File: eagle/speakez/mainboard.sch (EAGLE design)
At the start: 41 parts, among them U1 +12v

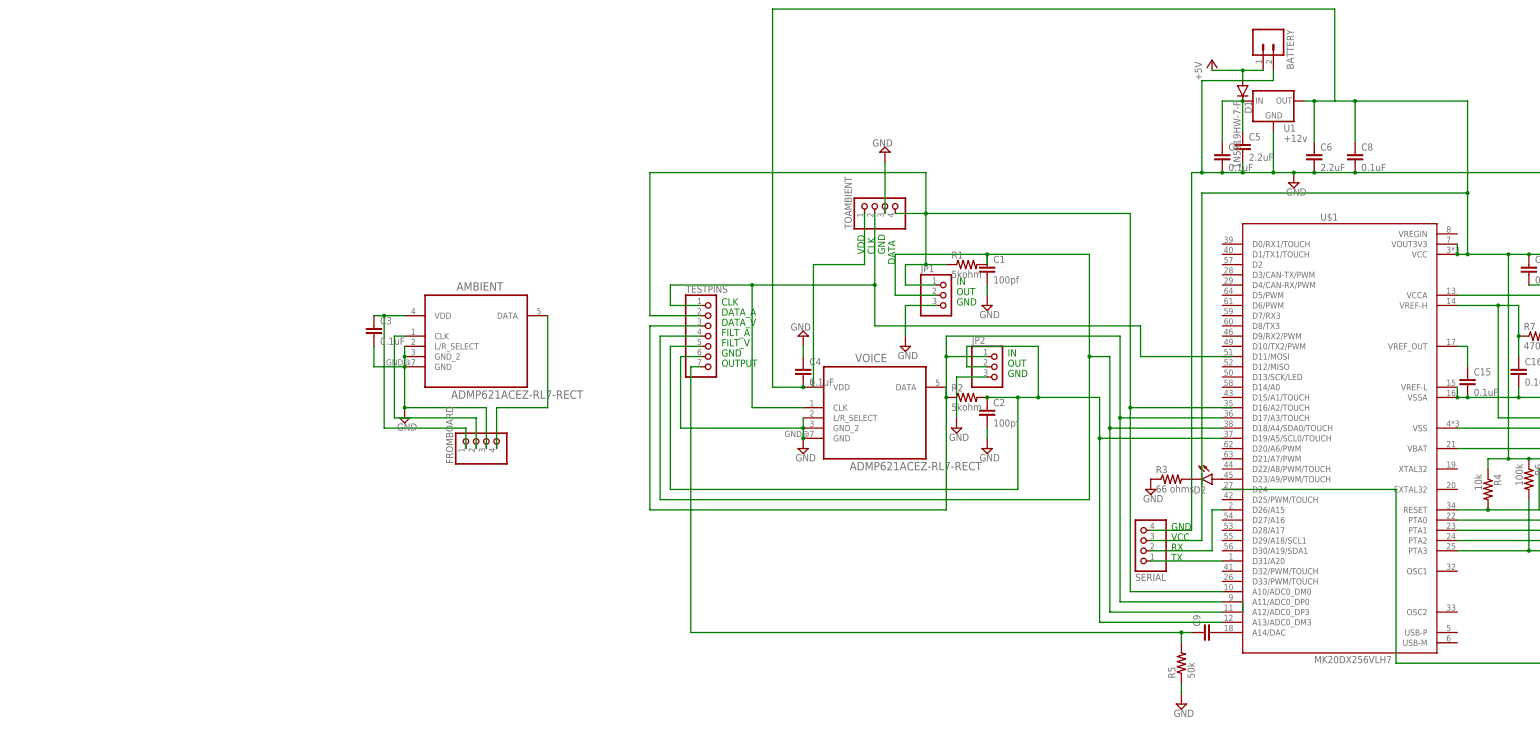
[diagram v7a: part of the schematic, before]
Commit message: corrected battery and voltage regulator
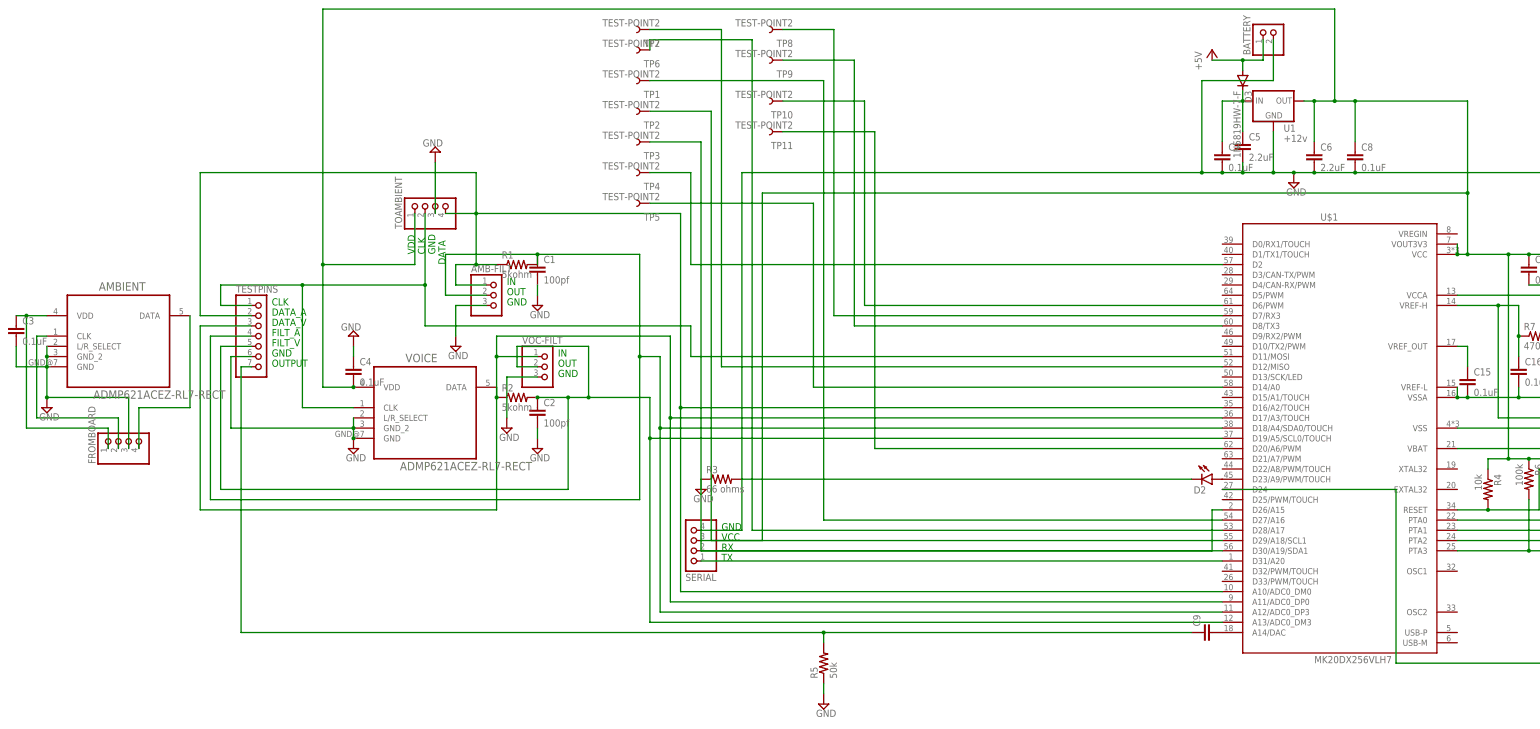
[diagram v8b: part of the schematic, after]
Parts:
- removed D1: 1N5819HW-7-F, SparkFun-DiscreteSemi:DIODESOD123
- removed JP1, JP2: (no value), pinhead:PINHD-1X3
- added AMB-FILT, VOC-FILT: (no value), pinhead:PINHD-1X3
- added D3: 1N5819HW-7-F, SparkFun-DiscreteSemi:DIODESOD123
- added TP1, TP10, TP11, TP2, TP3, TP4, TP5, TP6, TP7, TP8, TP9: TEST-POINT2, SparkFun-Passives:TEST-POINT2
- BATTERY: device SparkFun-Connectors:M02-JST-2-PTH-NO_SILK -> pinhead:PINHD-1X2
- U1: device SparkFun-PowerIC:V_REG_78XX7812 -> LP38691:V_REG_78XX7812
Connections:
- net N$6 renamed CLK2-A
- net N$7 renamed VDD-DECOUP-A
- net N$8 renamed DATA2-A
- removed net DECOUPLED: BK2125HM601-T.1, C10.1, C11.1, C12.1, C13.1, C14.1, C4.2, C6.1, C8.1, JLINK.1, R4.1, R6.1, SERIAL.3, TEST2.1, TEST2.6, TEST2.7, U$1.VBAT, U$1.VCC, U$1.VOUT3V3, U1.OUT, VOICE.VDD
- removed net TEST-PINS: TESTPINS.1, TOAMBIENT.2, VOICE.CLK
- new net CLK: TESTPINS.1, TOAMBIENT.2, U$1.D11/MOSI, VOICE.CLK
- new net DATA2: AMB-FILT.1, R1.1, TESTPINS.2, TOAMBIENT.4, U$1.A10/ADC0_DM0, U$1.D16/A2/TOUCH
- new net N$12: TP9.1, U$1.D8/TX3
- new net N$18: TP10.1, U$1.D6/PWM
- new net N$21: TP11.1, U$1.D20/A6/PWM
- new net N$3: TP7.1, U$1.D12/MISO
- new net N$4: TP6.1, U$1.D28/A17
- new net N$5: TP1.1, U$1.D27/A16
- new net N$6: TP2.1, U$1.D29/A18/SCL1
- new net N$7: TP3.1, U$1.D30/A19/SDA1
- new net N$8: TP4.1, U$1.D2
- new net VDD-DECOUP: BK2125HM601-T.1, C10.1, C11.1, C12.1, C13.1, C14.1, C4.2, C6.1, C8.1, JLINK.1, R4.1, R6.1, SERIAL.3, TEST2.1, TEST2.6, TEST2.7, TOAMBIENT.1, U$1.VBAT, U$1.VCC, U$1.VOUT3V3, U1.OUT, VOICE.VDD
- net +5V: now also D3.A; no longer D1.A
- net DATA: now also VOC-FILT.1; no longer JP2.1
- net GND: now also AMB-FILT.3, VOC-FILT.3; no longer JP1.3, JP2.3
- net N$1: now also AMB-FILT.2; no longer JP1.2
- net N$10: now also TP8.1, U$1.D7/RX3; no longer JP1.1, R1.1, TESTPINS.2, TOAMBIENT.4, U$1.A10/ADC0_DM0
- net N$15: now also D3.C; no longer D1.C
- net N$2: now also VOC-FILT.2; no longer JP2.2
- net N$9: now also TP5.1, U$1.D14/A0; no longer TOAMBIENT.1
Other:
- moved on the sheet: AMBIENT, BATTERY, C1, C2, C3, C4, FROMBOARD, R1, R2, R3, R5, SERIAL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
